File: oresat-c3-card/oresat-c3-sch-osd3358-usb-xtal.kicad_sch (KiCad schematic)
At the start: 45 parts, among them Q12 PMV45EN, Q2 NTR4101P, U1 OSD3358-1G-ISM, U11 RCLAMP0504FB, U43 FSUSB42MUX, Y1 ECS-240-12-30BQ-AEN-TR, Y2 ABS07-32.768KHZ-T

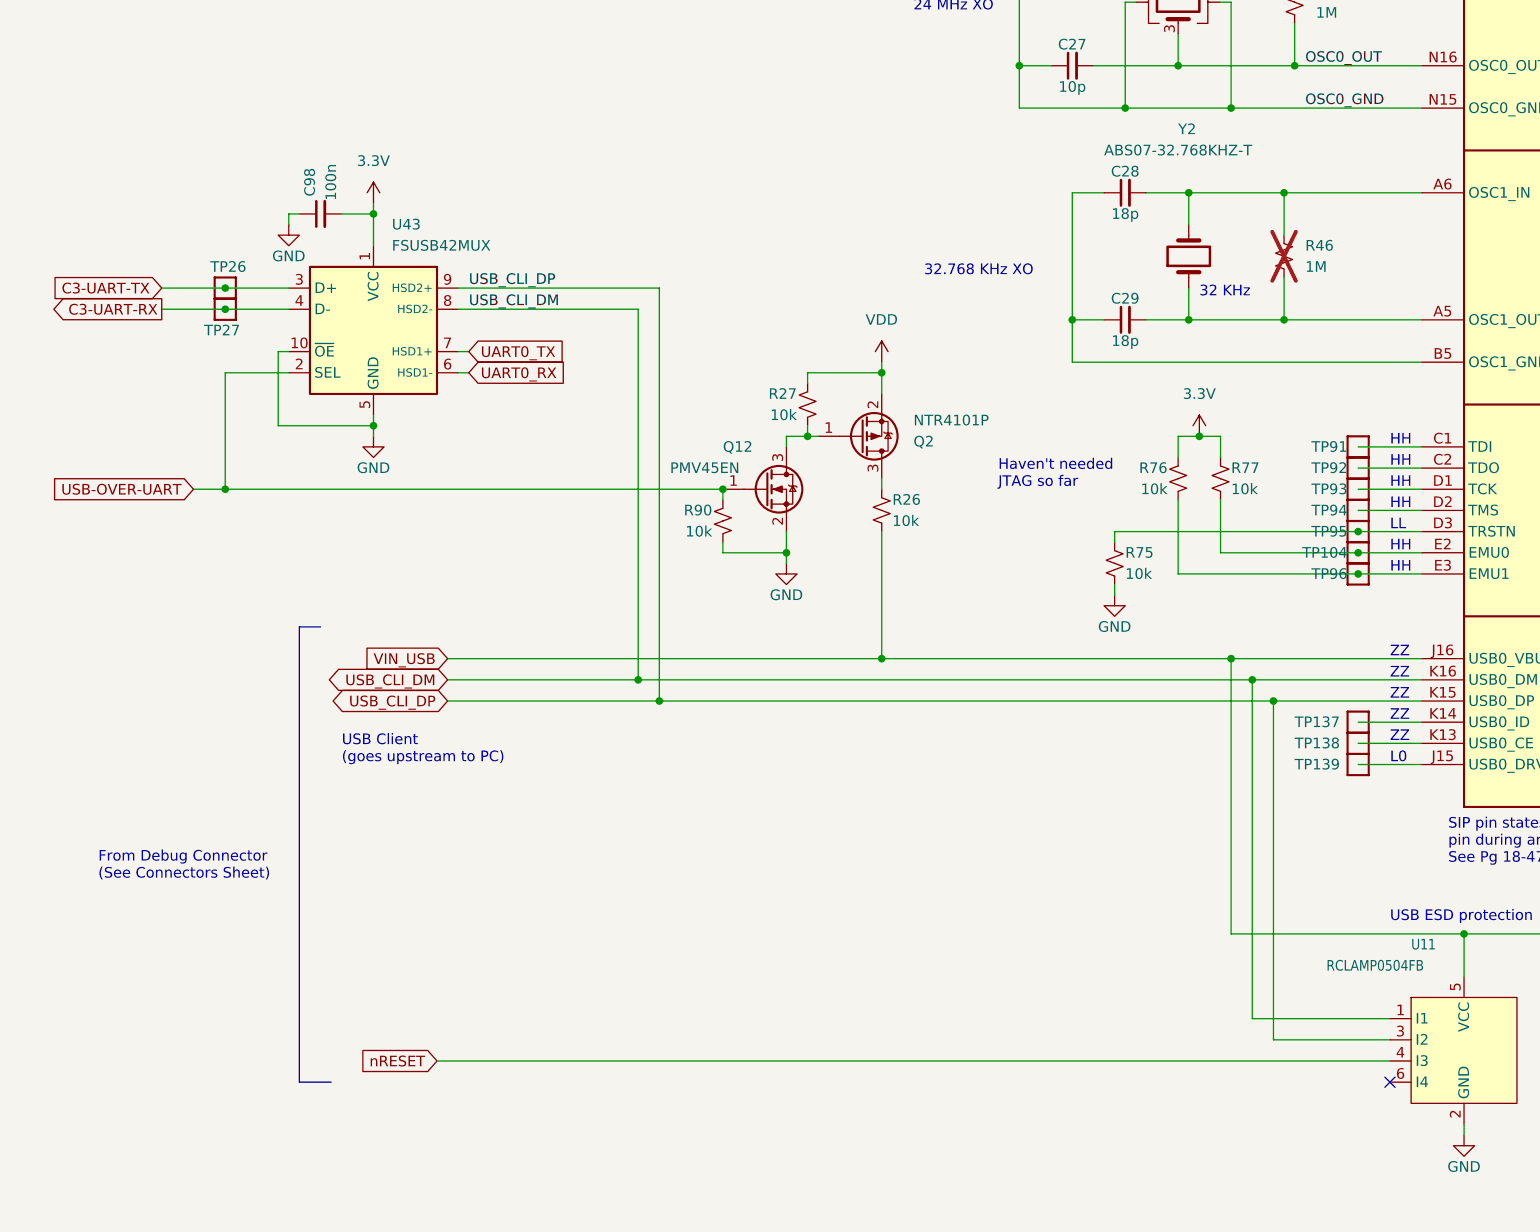
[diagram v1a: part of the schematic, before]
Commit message: schematic changes following design review
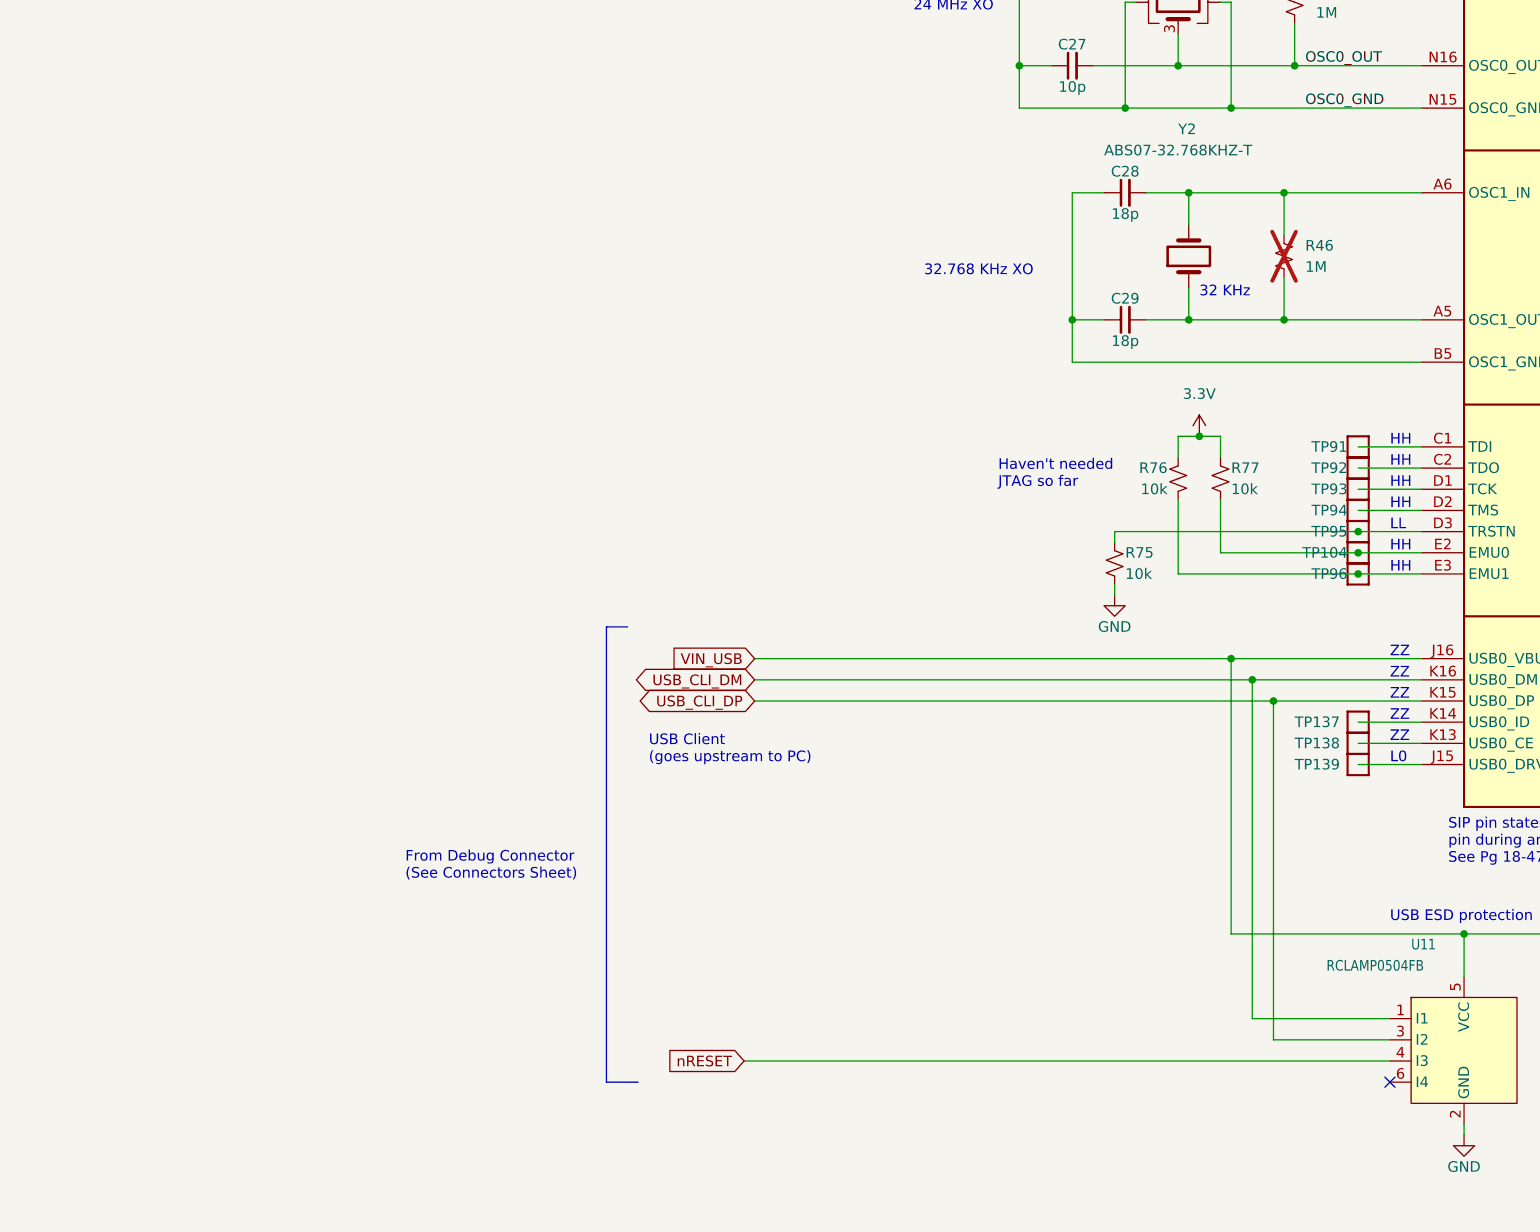
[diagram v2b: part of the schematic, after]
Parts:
- removed C98: 100n, Capacitor_SMD:C_0603_1608Metric, symbol Device:C_Small
- removed Q12: PMV45EN, Package_TO_SOT_SMD:SOT-23-3, symbol Device:Q_NMOS_GSD
- removed Q2: NTR4101P, Package_TO_SOT_SMD:SOT-23, symbol Transistor_FET:NTR2101P
- removed R26, R27, R90: 10k, Resistor_SMD:R_0603_1608Metric, symbol Device:R_Small_US
- removed TP26, TP27: Test-Point, oresat-misc:TestPoint_Pad_D1.0mm, symbol oresat-misc:Test-Point-1mm-round
- removed U43: FSUSB42MUX, Package_SO:MSOP-10_3x3mm_P0.5mm, symbol Interface_USB:FSUSB42MUX

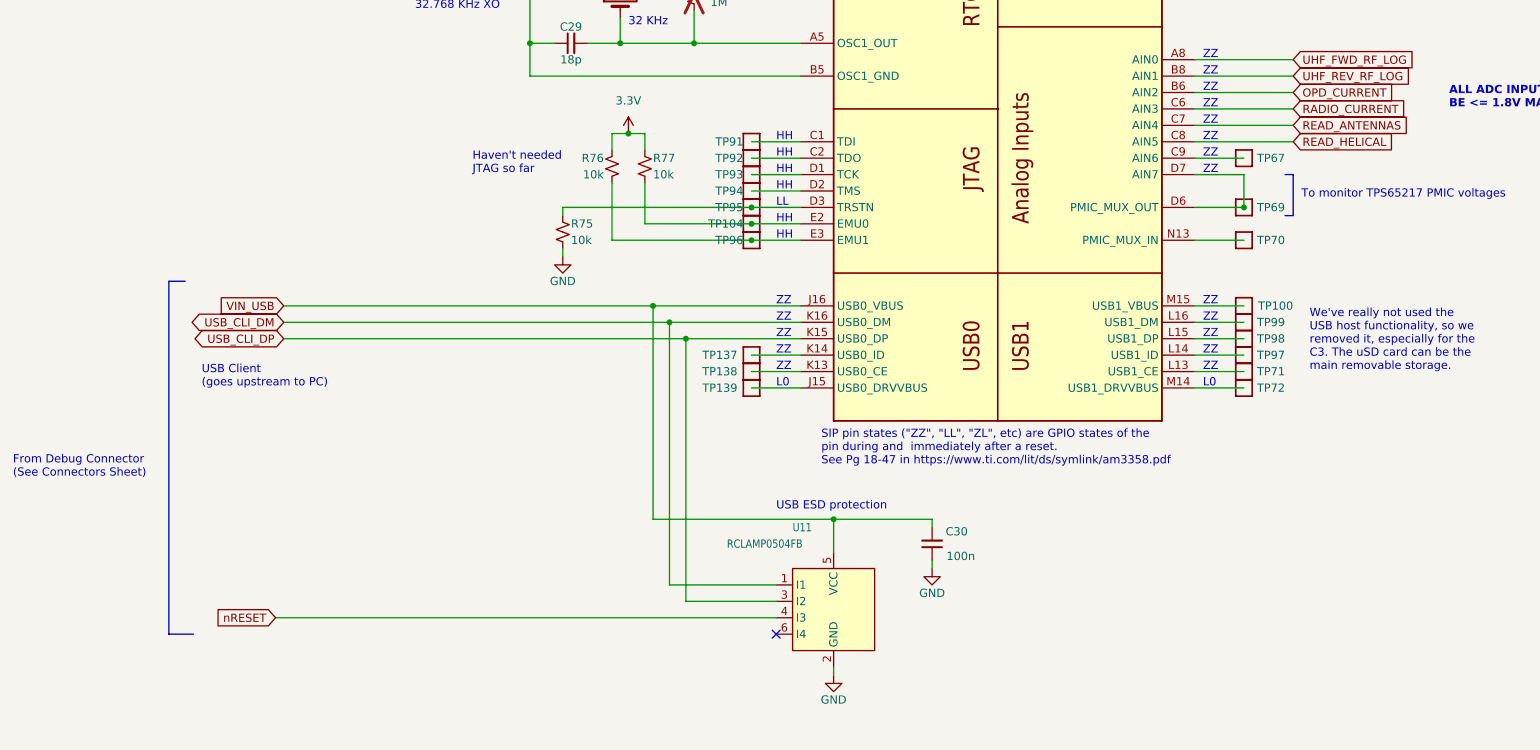
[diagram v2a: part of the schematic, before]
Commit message: Additional C3 design review changes and routing progress
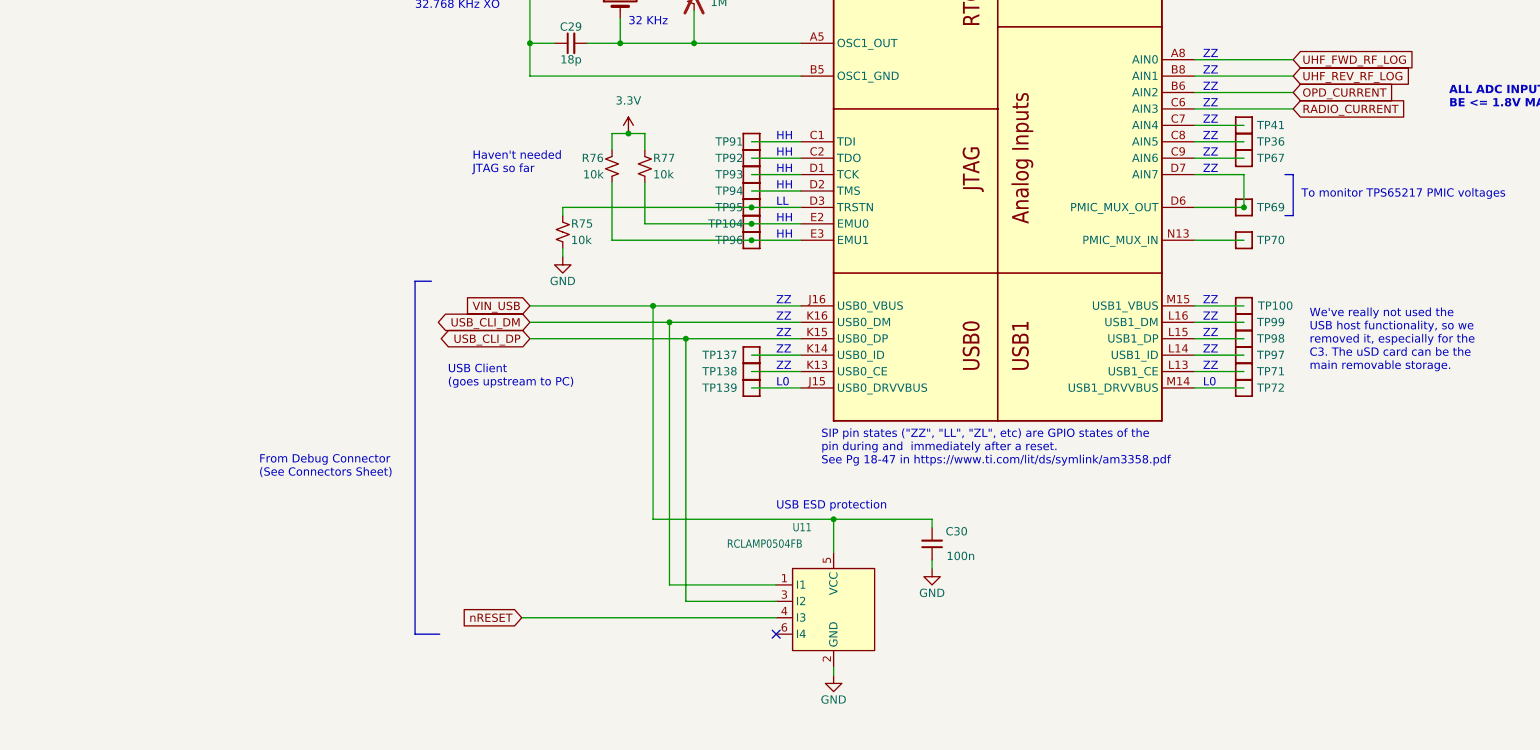
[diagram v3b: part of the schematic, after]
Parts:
- added TP36, TP41: Test-Point, oresat-misc:TestPoint_Pad_D1.0mm, symbol oresat-misc:Test-Point-1mm-round
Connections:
- net READ_ANTENNAS: no longer names the net of U1.C7 (AIN4)
- net READ_ANTENNAS: now also TP41.1
- net READ_HELICAL: no longer names the net of U1.C8 (AIN5)
- net READ_HELICAL: now also TP36.1
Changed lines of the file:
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@@
 	(text "USB Client\n(goes upstream to PC)"
 		(exclude_from_sim no)
-		(at 102.87 172.72 0)
+		(at 140.97 172.72 0)
 		(effects
 			(font
@@
 	(text "From Debug Connector\n(See Connectors Sheet)"
 		(exclude_from_sim no)
-		(at 73.66 186.69 0)
+		(at 111.76 186.69 0)
 		(effects
 			(font
@@
 	(polyline
 		(pts
-			(xy 97.79 156.21) (xy 97.79 210.82)
+			(xy 135.89 156.21) (xy 135.89 210.82)
 		)
 		(stroke
@@
 	(wire
 		(pts
-			(xy 256.54 132.08) (xy 271.78 132.08)
+			(xy 256.54 132.08) (xy 264.16 132.08)
 		)
 		(stroke
@@
 	(wire
 		(pts
-			(xy 115.57 165.1) (xy 177.8 165.1)
+			(xy 153.67 165.1) (xy 177.8 165.1)
 		)
 		(stroke
@@
 	(wire
 		(pts
-			(xy 115.57 162.56) (xy 175.26 162.56)
+			(xy 153.67 162.56) (xy 175.26 162.56)
 		)
 		(stroke
@@
 	(polyline
 		(pts
-			(xy 100.33 156.21) (xy 97.79 156.21)
+			(xy 138.43 156.21) (xy 135.89 156.21)
 		)
 		(stroke
@@
 	(wire
 		(pts
-			(xy 114.3 208.28) (xy 191.77 208.28)
+			(xy 152.4 208.28) (xy 191.77 208.28)
 		)
 		(stroke
@@
 	(wire
 		(pts
-			(xy 115.57 160.02) (xy 172.72 160.02)
+			(xy 153.67 160.02) (xy 172.72 160.02)
 		)
 		(stroke
@@
 	(wire
 		(pts
-			(xy 256.54 134.62) (xy 271.78 134.62)
+			(xy 256.54 134.62) (xy 264.16 134.62)
 		)
 		(stroke
@@
 	(polyline
 		(pts
-			(xy 97.79 210.82) (xy 101.6 210.82)
+			(xy 135.89 210.82) (xy 139.7 210.82)
 		)
 		(stroke
@@
 	(global_label "USB_CLI_DP"
 		(shape bidirectional)
-		(at 115.57 165.1 180)
+		(at 153.67 165.1 180)
 		(effects
 			(font
@@
 		)
 		(property "Intersheetrefs" "${INTERSHEET_REFS}"
-			(at 101.6 165.1 0)
+			(at 139.7 165.1 0)
 			(effects
 				(font
@@
 	(global_label "nRESET"
 		(shape input)
-		(at 114.3 208.28 180)
+		(at 152.4 208.28 180)
 		(effects
 			(font
@@
 		)
 		(property "Intersheetrefs" "${INTERSHEET_REFS}"
-			(at 104.14 208.28 0)
+			(at 142.24 208.28 0)
 			(effects
 				(font
@@
 	(global_label "USB_CLI_DM"
 		(shape bidirectional)
-		(at 115.57 162.56 180)
+		(at 153.67 162.56 180)
 		(effects
 			(font
@@
 		)
 		(property "Intersheetrefs" "${INTERSHEET_REFS}"
-			(at 101.6 162.56 0)
+			(at 139.7 162.56 0)
 			(effects
 				(font
@@
 		)
 	)
-	(global_label "READ_HELICAL"
-		(shape input)
-		(at 271.78 134.62 0)
-		(fields_autoplaced yes)
-		(effects
-			(font
-				(size 1.27 1.27)
-			)
-			(justify left)
-		)
-		(property "Intersheetrefs" "${INTERSHEET_REFS}"
-			(at 287.9301 134.62 0)
-			(effects
-				(font
-					(size 1.27 1.27)
-				)
-				(justify left)
-			)
-		)
-	)
 	(global_label "UHF_FWD_RF_LOG"
 		(shape input)
@@
 		)
 	)
-	(global_label "READ_ANTENNAS"
-		(shape input)
-		(at 271.78 132.08 0)
-		(fields_autoplaced yes)
-		(effects
-			(font
-				(size 1.27 1.27)
-			)
-			(justify left)
-		)
-		(property "Intersheetrefs" "${INTERSHEET_REFS}"
-			(at 289.9258 132.08 0)
-			(effects
-				(font
-					(size 1.27 1.27)
-				)
-				(justify left)
-			)
-		)
-	)
 	(global_label "UHF_REV_RF_LOG"
 		(shape input)
@@
 	(global_label "VIN_USB"
 		(shape input)
-		(at 115.57 160.02 180)
+		(at 153.67 160.02 180)
 		(fields_autoplaced yes)
 		(effects
@@
 		)
 		(property "Intersheetrefs" "${INTERSHEET_REFS}"
-			(at 105.3555 159.9406 0)
+			(at 143.4555 159.9406 0)
 			(effects
 				(font
@@
 	(symbol
 		(lib_id "oresat-misc:Test-Point-1mm-round")
+		(at 264.16 132.08 180)
+		(unit 1)
+		(exclude_from_sim yes)
+		(in_bom no)
+		(on_board yes)
+		(dnp no)
+		(property "Reference" "TP41"
+			(at 270.51 132.08 0)
+			(effects
+				(font
+					(size 1.27 1.27)
+				)
+				(justify left)
+			)
+		)
+		(property "Value" "Test-Point"
+			(at 264.16 134.62 0)
+			(effects
+				(font
+					(size 1.27 1.27)
+				)
+				(hide yes)
+			)
+		)
+		(property "Footprint" "oresat-misc:TestPoint_Pad_D1.0mm"
+			(at 264.16 142.24 0)
+			(effects
+				(font
+					(size 1.27 1.27)
+				)
+				(hide yes)
+			)
+		)
+		(property "Datasheet" ""
+			(at 264.16 132.08 0)
+			(effects
+				(font
+					(size 1.27 1.27)
+				)
+				(hide yes)
+			)
+		)
+		(property "Description" "1mm round SMT test point"
+			(at 264.16 132.08 0)
+			(effects
+				(font
+					(size 1.27 1.27)
+				)
+				(hide yes)
+			)
+		)
+		(pin "1"
+		)
+		(instances
+			(project "oresat-c3"
+				(path "/65d12cdd-c326-4033-9053-c59fa4e0b25e/0d3a1fa4-c9ee-4335-9068-a81ae0178f3f"
+					(reference "TP41")
+					(unit 1)
+				)
+			)
+		)
+	)
+	(symbol
+		(lib_id "oresat-misc:Test-Point-1mm-round")
 		(at 187.96 134.62 180)
 		(unit 1)
@@
 					(unit 1)
 				)
+			)
+		)
+	)
+	(symbol
+		(lib_id "oresat-misc:Test-Point-1mm-round")
+		(at 264.16 134.62 180)
+		(unit 1)
+		(exclude_from_sim yes)
+		(in_bom no)
+		(on_board yes)
+		(dnp no)
+		(property "Reference" "TP36"
+			(at 270.51 134.62 0)
+			(effects
+				(font
+					(size 1.27 1.27)
+				)
+				(justify left)
+			)
+		)
+		(property "Value" "Test-Point"
+			(at 264.16 137.16 0)
+			(effects
+				(font
+					(size 1.27 1.27)
+				)
+				(hide yes)
+			)
+		)
+		(property "Footprint" "oresat-misc:TestPoint_Pad_D1.0mm"
+			(at 264.16 144.78 0)
+			(effects
+				(font
+					(size 1.27 1.27)
+				)
+				(hide yes)
+			)
+		)
+		(property "Datasheet" ""
+			(at 264.16 134.62 0)
+			(effects
+				(font
+					(size 1.27 1.27)
+				)
+				(hide yes)
+			)
+		)
+		(property "Description" "1mm round SMT test point"
+			(at 264.16 134.62 0)
+			(effects
+				(font
+					(size 1.27 1.27)
+				)
+				(hide yes)
+			)
+		)
+		(pin "1"
+		)
+		(instances
+			(project "oresat-c3"
+				(path "/65d12cdd-c326-4033-9053-c59fa4e0b25e/0d3a1fa4-c9ee-4335-9068-a81ae0178f3f"
+					(reference "TP36")
+					(unit 1)
+				)

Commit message: Design review on power and RF
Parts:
- U1: Distributor (none) -> DigiKey; MPN OSD3358-1G-ISM -> OSD3358-512M-BSM
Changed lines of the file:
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@@
 	)
 	(junction
-		(at 172.72 93.98)
-		(diameter 0)
-		(color 0 0 0 0)
-	)
-	(junction
 		(at 175.26 162.56)
 		(diameter 0)
@@
 	(wire
 		(pts
-			(xy 171.45 81.28) (xy 172.72 81.28)
-		)
-		(stroke
-			(width 0)
-			(type default)
-		)
-	)
-	(wire
-		(pts
 			(xy 166.37 85.09) (xy 166.37 88.9)
 		)
@@
 	(wire
 		(pts
-			(xy 172.72 81.28) (xy 172.72 93.98)
-		)
-		(stroke
-			(width 0)
-			(type default)
-		)
-	)
-	(wire
-		(pts
 			(xy 180.34 73.66) (xy 180.34 78.74)
 		)
@@
 	(wire
 		(pts
-			(xy 160.02 93.98) (xy 172.72 93.98)
+			(xy 160.02 93.98) (xy 195.58 93.98)
 		)
 		(stroke
@@
 	(wire
 		(pts
-			(xy 172.72 93.98) (xy 195.58 93.98)
-		)
-		(stroke
-			(width 0)
-			(type default)
-		)
-	)
-	(wire
-		(pts
 			(xy 256.54 71.12) (xy 261.62 71.12)
 		)
@@
 			)
 		)
-		(property "Datasheet" "https://ecsxtal.com/store/pdf/ECX-53BQ.pdf"
+		(property "Datasheet" "~"
 			(at 166.37 81.28 0)
 			(effects
@@
 			)
 		)
-		(property "Description" "CRYSTAL 24.0000MHZ 12PF SMD"
+		(property "Description" "Four pin crystal, GND on pins 2 and 4"
 			(at 166.37 81.28 0)
 			(effects
@@
 			)
 		)
-		(property "Description" "Embedded Module ARM® Cortex®-A8, AM3358 1GHz 1GB"
+		(property "Description" "OSD335x Embedded Module 1GHz 512MB"
 			(at 226.06 12.7 0)
 			(effects
@@
 			)
 		)
-		(property "MPN" "OSD3358-1G-ISM"
+		(property "MPN" "OSD3358-512M-BSM"
 			(at 226.06 17.78 0)
 			(effects
@@
 			(effects
 				(font
+					(size 1.27 1.27)
+				)
+				(hide yes)
+			)
+		)
+		(property "Distributor" "DigiKey"
+			(at 226.06 15.24 0)
+			(effects
+				(font
